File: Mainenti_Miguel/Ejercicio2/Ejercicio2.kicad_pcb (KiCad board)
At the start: 2 copper layers, 40.6 x 61 mm, 13 parts, among them J1 DB9, U1 AMIS42665TJAA1RG, U2 SP3232

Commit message: ruteado y con 3d
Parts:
- moved JP1 0.52 mm to (126.4, 115.7)
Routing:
- net GND: track 3.39 -> 53.8 mm, vias 0 -> 17
- net Net-(JP1-Pad2): track 21.8 -> 21.0 mm
- net Net-(C4-Pad2): track 8.61 -> 7.88 mm
- added copper zone on B.Cu, net GND
- added copper zone on F.Cu, net GND
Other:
- board text added: "INDUSTRIA ARGENTINA"

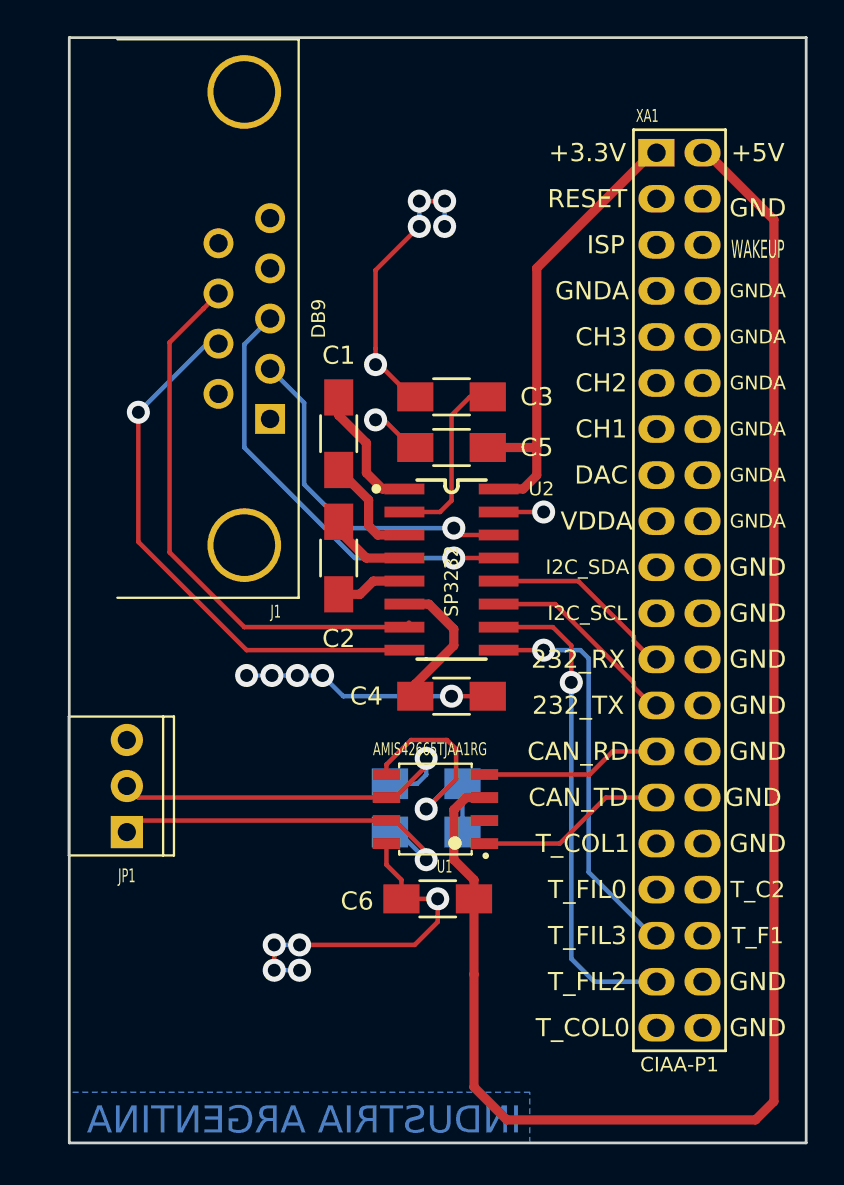
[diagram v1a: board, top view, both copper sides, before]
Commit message: se agregaron logos y licencia. Se activaron capas de cobre que estaban desactivadas
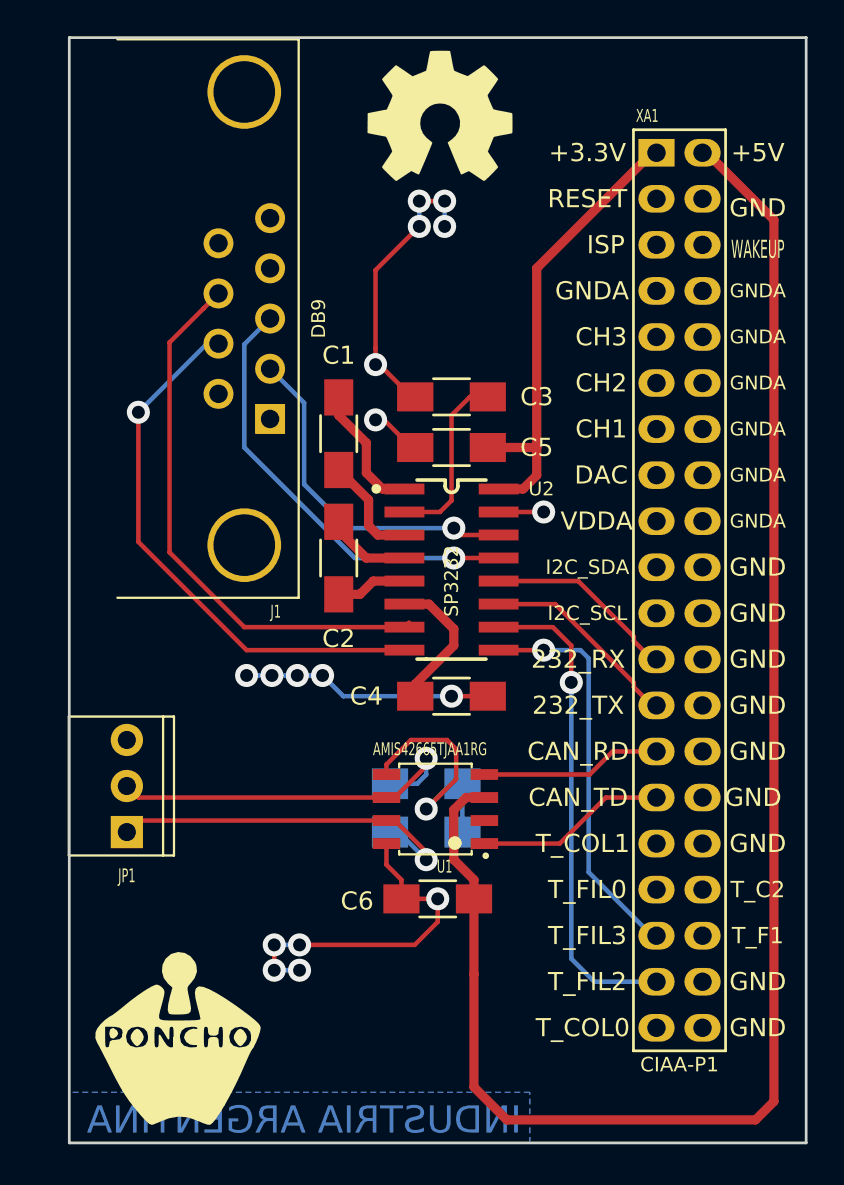
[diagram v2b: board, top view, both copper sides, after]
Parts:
- added G***: LOGO, ej2:Logo_Poncho, F.Cu at (129.2, 129.7)
- added G101: Logo_OSHWA, ej2:Logo_OSHWA, F.Cu at (143.6, 78.7)

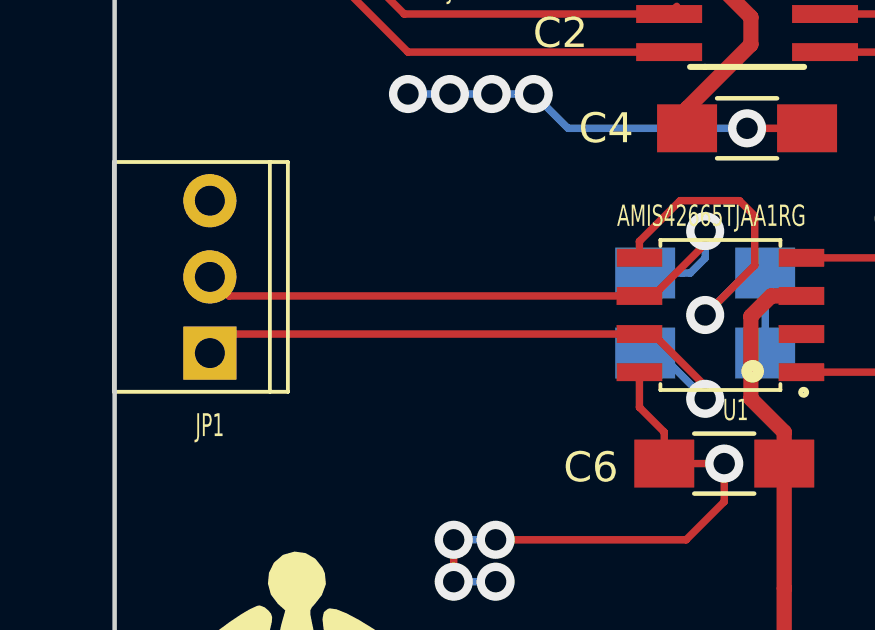
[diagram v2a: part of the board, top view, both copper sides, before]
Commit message: ruteo del par diferencial y ecualizado
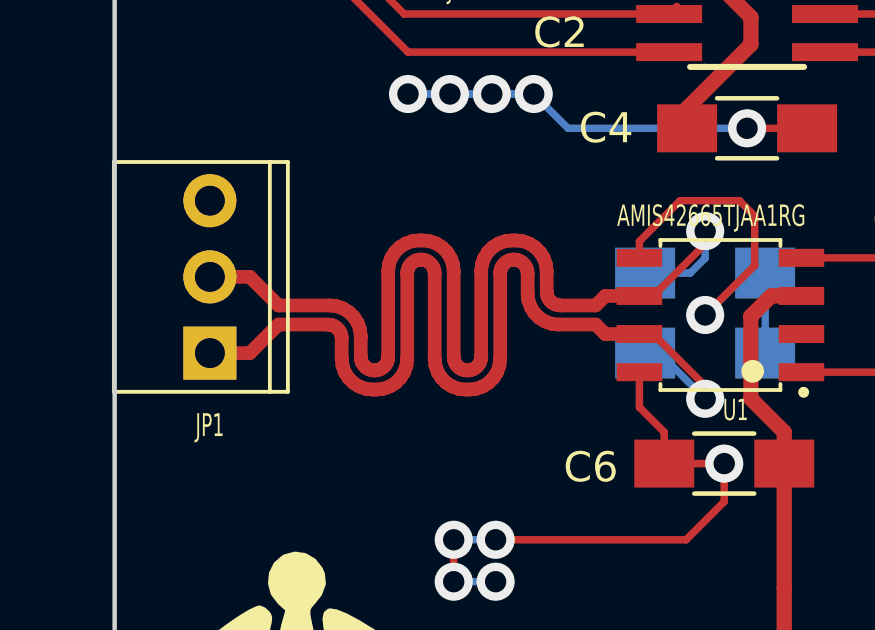
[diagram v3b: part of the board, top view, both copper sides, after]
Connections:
- net Net-(JP1-Pad1) renamed /Conector y Can/CAN_P
- net Net-(JP1-Pad2) renamed /Conector y Can/CAN_N
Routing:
- net /Conector y Can/CAN_P: track 20.5 -> 35.8 mm
- net /Conector y Can/CAN_N: track 21.0 -> 35.4 mm
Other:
- net class Default: clearance 0.2 -> 0.1524
- rule trace_clearance: 0.2 -> 0.1524
- board text added: "1 Oz"
- board text added: "1,6 mm"
- board text added: "Dieléctrico"
- board text added: "L1 TOP (Mixed)"
- board text added: "L2 BOT (Mixed)"
- board text added: "STACK-UP:"
- board text added: "Terminación superficial: HASL Espesor final aprox.: 1,6mm"
